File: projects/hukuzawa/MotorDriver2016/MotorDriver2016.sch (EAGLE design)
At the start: 54 parts, among them IC1 PIC16F648, IC2 TLP521, IC3 TLP521, J3 3PIN(L), J4 3PIN(L)

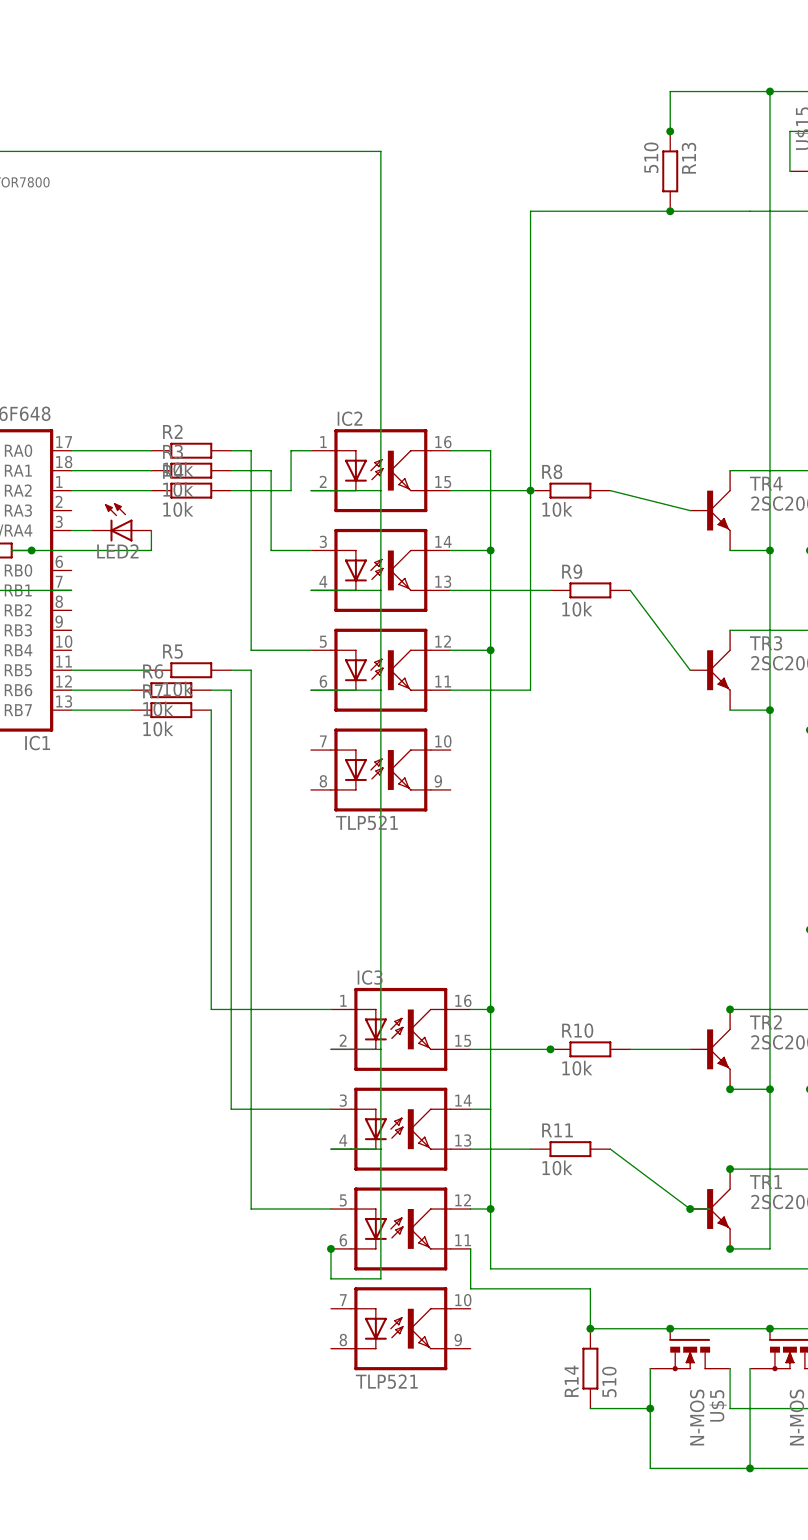
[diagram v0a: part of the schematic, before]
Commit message: 旧モータードライバ更新
使用抵抗の値を変更
イメージファイルにエクスポート
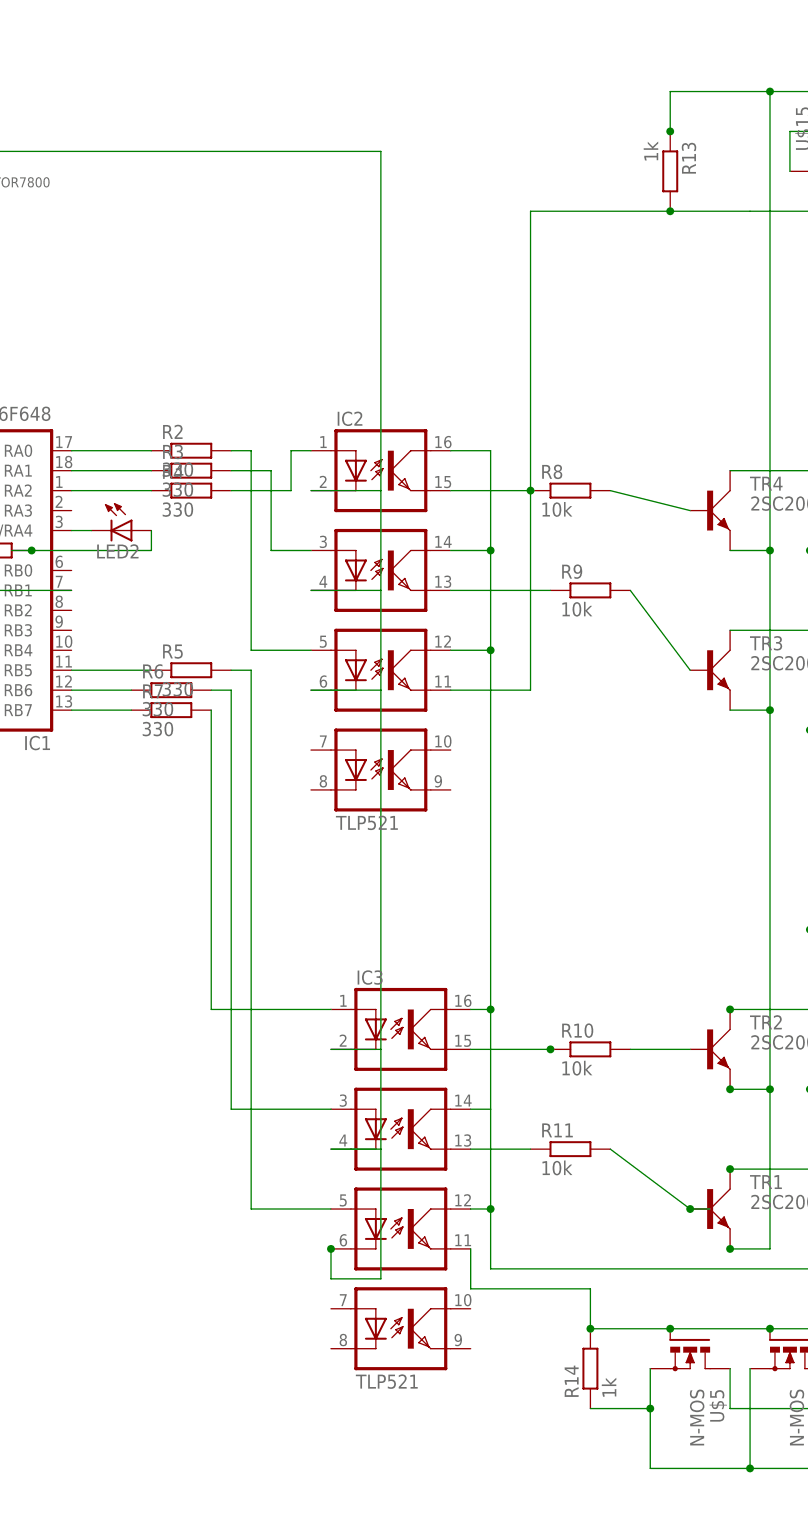
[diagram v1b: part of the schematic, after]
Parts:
- R13, R14: value 510 -> 1k
- R2, R3, R4, R5, R6, R7: value 10k -> 330
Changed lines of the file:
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@@
 <part name="R10" library="rcl" deviceset="R-EU_" device="R3216W" value="10k"/>
 <part name="R11" library="rcl" deviceset="R-EU_" device="R3216W" value="10k"/>
-<part name="R13" library="rcl" deviceset="R-EU_" device="R3216W" value="510"/>
+<part name="R13" library="rcl" deviceset="R-EU_" device="R3216W" value="1k"/>
 <part name="TR1" library="My_transistor" deviceset="2SC2001" device=""/>
 <part name="TR2" library="My_transistor" deviceset="2SC2001" device=""/>
@@
 <part name="R1" library="rcl" deviceset="R-EU_" device="R3216W" value="2k"/>
 <part name="IC1" library="FP-21T for MITS" deviceset="PIC16F648" device=""/>
-<part name="R2" library="rcl" deviceset="R-EU_" device="R3216W" value="10k"/>
-<part name="R3" library="rcl" deviceset="R-EU_" device="R3216W" value="10k"/>
-<part name="R4" library="rcl" deviceset="R-EU_" device="R3216W" value="10k"/>
-<part name="R5" library="rcl" deviceset="R-EU_" device="R3216W" value="10k"/>
-<part name="R6" library="rcl" deviceset="R-EU_" device="R3216W" value="10k"/>
-<part name="R7" library="rcl" deviceset="R-EU_" device="R3216W" value="10k"/>
+<part name="R2" library="rcl" deviceset="R-EU_" device="R3216W" value="330"/>
+<part name="R3" library="rcl" deviceset="R-EU_" device="R3216W" value="330"/>
+<part name="R4" library="rcl" deviceset="R-EU_" device="R3216W" value="330"/>
+<part name="R5" library="rcl" deviceset="R-EU_" device="R3216W" value="330"/>
+<part name="R6" library="rcl" deviceset="R-EU_" device="R3216W" value="330"/>
+<part name="R7" library="rcl" deviceset="R-EU_" device="R3216W" value="330"/>
 <part name="IC2" library="FP-21T for MITS" deviceset="TLP521" device=""/>
 <part name="IC3" library="FP-21T for MITS" deviceset="TLP521" device=""/>
@@
 <part name="U$3" library="My_rcl" deviceset="C-ELEC" device=""/>
 <part name="C1" library="My_rcl" deviceset="C-" device=""/>
-<part name="R14" library="rcl" deviceset="R-EU_" device="R3216W" value="510"/>
+<part name="R14" library="rcl" deviceset="R-EU_" device="R3216W" value="1k"/>
 <part name="U$5" library="FET_kai" deviceset="N-MOS" device=""/>
 <part name="U$10" library="FET_kai" deviceset="N-MOS" device=""/>
